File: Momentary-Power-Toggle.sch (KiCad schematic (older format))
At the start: 14 parts, among them J1 PWR_C, J2 PWR_2, J3 BT-, Q1 IRF7317PbF, SW1 ON / OFF Button

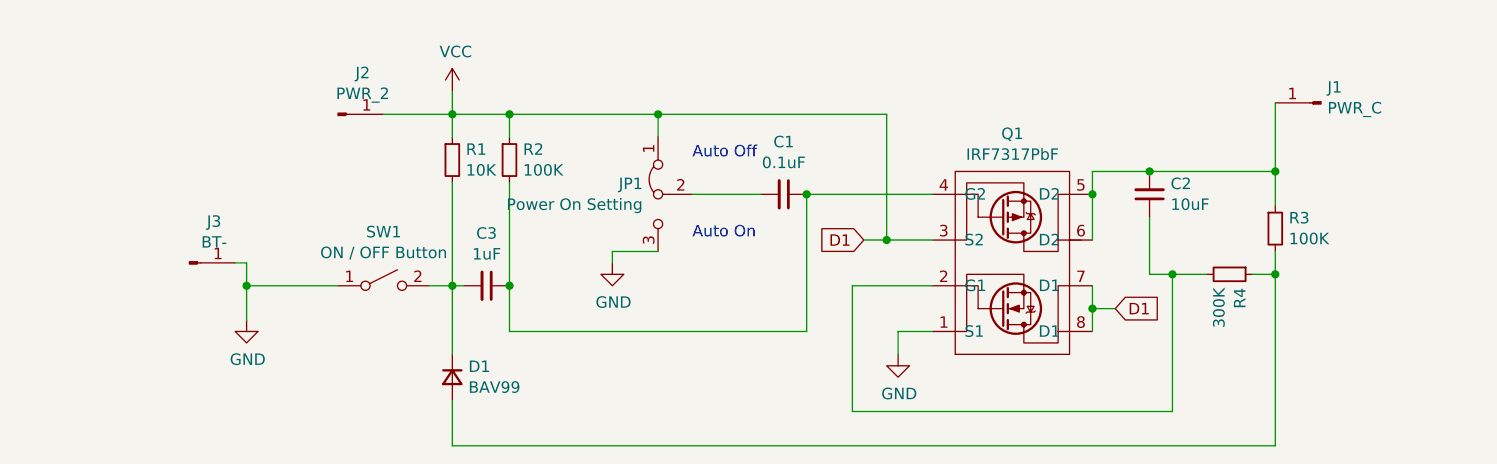
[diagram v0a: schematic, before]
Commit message: Add files via upload
fixed schematic error
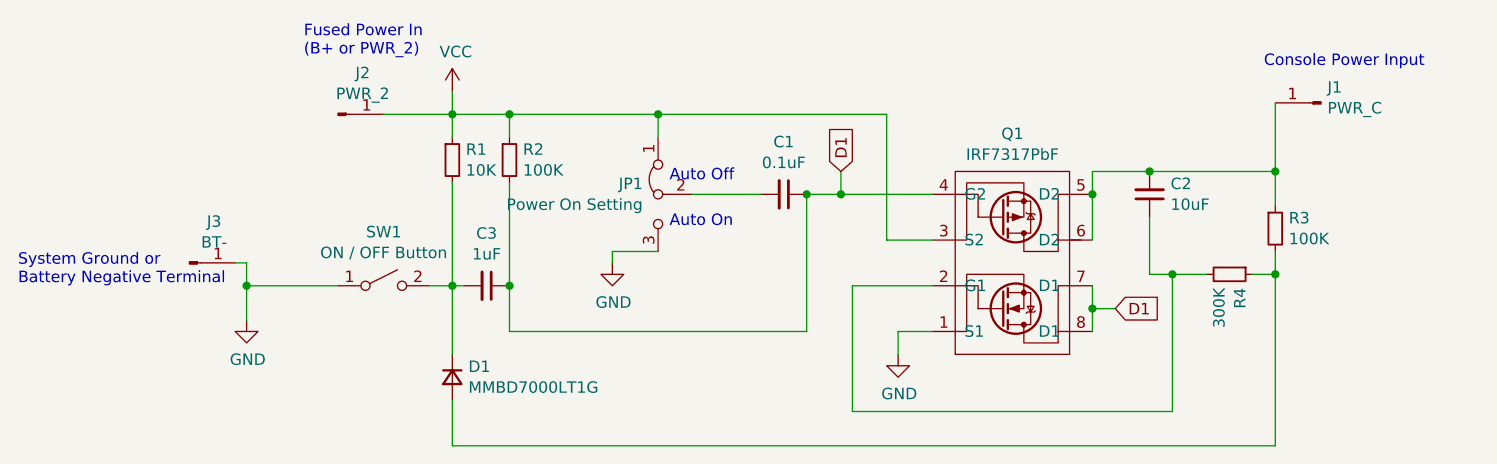
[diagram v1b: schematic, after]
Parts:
- D1: value BAV99 -> MMBD7000LT1G
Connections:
- net VCC: no longer Q1.7 (D1), Q1.8 (D1)
- net D1: now reaches C1.1, C3.1, Q1.4 (G2), R2.2
- net D1: now also Q1.7 (D1), Q1.8 (D1)
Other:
- note added: "Console Power Input"
- note added: "Fused Power In\n(B+ or PWR_2)"
- note added: "System Ground or \nBattery Negative Terminal"
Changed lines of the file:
@@
 P 3550 3850
 F 0 "D1" V 3504 3920 50  0000 L CNN
-F 1 "BAV99" V 3595 3920 50  0000 L CNN
+F 1 "MMBD7000LT1G" V 3595 3920 50  0000 L CNN
 F 2 "Diode_SMD:D_SOT-23_ANK" V 3550 3850 50  0001 C CNN
 F 3 "~" V 3550 3850 50  0001 C CNN
@@
 	1    0    0    -1
 $EndComp
-Text Notes 4600 3250 0    50   ~ 0
+Text Notes 4500 3200 0    50   ~ 0
 Auto On
-Text Notes 4600 2900 0    50   ~ 0
+Text Notes 4500 3000 0    50   ~ 0
 Auto Off
 $Comp
@@
 	5450 3250 5650 3250
 Wire Wire Line
-	5650 3050 5100 3050
+	5650 3050 5250 3050
 Wire Wire Line
 	6350 3250 6350 3050
@@
 Wire Wire Line
 	6350 3550 6350 3650
-Text GLabel 5350 3250 0    50   Input ~ 0
+Text GLabel 5250 2950 1    50   Input ~ 0
 D1
-Wire Wire Line
-	5350 3250 5450 3250
-Connection ~ 5450 3250
 Wire Wire Line
 	6600 3150 6600 3400
@@
 Wire Wire Line
 	3250 2700 3550 2700
+Text Notes 7100 2500 0    50   ~ 0
+Console Power Input
+Text Notes 1650 3450 0    50   ~ 0
+System Ground or \nBattery Negative Terminal
+Text Notes 2900 2450 0    50   ~ 0
+Fused Power In\n(B+ or PWR_2)
+Wire Wire Line
+	5250 2950 5250 3050
+Connection ~ 5250 3050
+Wire Wire Line
+	5250 3050 5100 3050
 $EndSCHEMATC

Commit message: general cleanup
defuckulated the repository by removing obsolete board configs, updating schematic image, condensing readmes, etc
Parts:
- removed JP1: Power On Setting, Jumper:SolderJumper-3_P1.3mm_Bridged2Bar12_RoundedPad1.0x1.5mm_NumberLabels, symbol Jumper:Jumper_3_Bridged12
- removed SW1: ON / OFF Button, Button_Switch_THT:SW_Tactile_SPST_Angled_PTS645Vx83-2LFS, symbol Switch:SW_SPST
- added J4: GND, TestPoint:TestPoint_Pad_1.5x1.5mm, symbol Connector:Conn_01x01_Male
- J3: value BT- -> BTN
- Q1: symbol misc:IRF7317PbF -> Momentary-Power-Toggle-rescue:IRF7317PbF-misc
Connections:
- net GND: now also J4.1 (Pin_1); no longer J3.1 (Pin_1)
- net VCC: now also C1.2
- net at C3.2, D1.1 (K), R1.2: now also J3.1 (Pin_1)
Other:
- note added: "Button to System \nGround or Battery \nNegative Terminal"
- note removed: "Auto Off"
- note removed: "Auto On"
- note removed: "System Ground or \nBattery Negative Terminal"
- moved on the sheet: J3
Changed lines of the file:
@@
-$EndComp
-$Comp
-L power:GND #PWR03
-U 1 1 5F3F1AD6
-P 2650 3600
-F 0 "#PWR03" H 2650 3350 50  0001 C CNN
-F 1 "GND" H 2655 3427 50  0000 C CNN
-F 2 "" H 2650 3600 50  0001 C CNN
-F 3 "" H 2650 3600 50  0001 C CNN
-	1    2650 3600
-	1    0    0    -1
-$EndComp
-$Comp
-L Switch:SW_SPST SW1
-U 1 1 5F3F1E0E
-P 3250 3450
-F 0 "SW1" H 3250 3685 50  0000 C CNN
-F 1 "ON / OFF Button" H 3250 3594 50  0000 C CNN
-F 2 "Button_Switch_THT:SW_Tactile_SPST_Angled_PTS645Vx83-2LFS" H 3250 3450 50  0001 C CNN
-F 3 "~" H 3250 3450 50  0001 C CNN
-	1    3250 3450
-	1    0    0    -1
 $EndComp
 $Comp
@@
 $EndComp
 $Comp
-L Jumper:Jumper_3_Bridged12 JP1
-U 1 1 5F3F302E
-P 4450 3050
-F 0 "JP1" V 4404 3117 50  0000 L CNN
-F 1 "Power On Setting" V 4495 3117 50  0000 L CNN
-F 2 "Jumper:SolderJumper-3_P1.3mm_Bridged2Bar12_RoundedPad1.0x1.5mm_NumberLabels" H 4450 3050 50  0001 C CNN
-F 3 "~" H 4450 3050 50  0001 C CNN
-	1    4450 3050
-	0    -1   1    0
-$EndComp
-$Comp
 L Device:D_Small D1
 U 1 1 5F3F351C
@@
 $EndComp
 $Comp
-L misc:IRF7317PbF Q1
+L Momentary-Power-Toggle-rescue:IRF7317PbF-misc Q1
 U 1 1 5F3FED7F
 P 6000 3300
@@
 	1    0    0    1
 $EndComp
-Wire Wire Line
-	3050 3450 2650 3450
 $Comp
 L Device:R_Small R2
@@
 	1    0    0    -1
 $EndComp
-Text Notes 4500 3200 0    50   ~ 0
-Auto On
-Text Notes 4500 3000 0    50   ~ 0
-Auto Off
 $Comp
 L Device:C_Small C1
@@
 	1    5000 3050
 	0    1    1    0
-$EndComp
-$Comp
-L power:GND #PWR02
-U 1 1 5F403AD7
-P 4250 3350
-F 0 "#PWR02" H 4250 3100 50  0001 C CNN
-F 1 "GND" H 4255 3177 50  0000 C CNN
-F 2 "" H 4250 3350 50  0001 C CNN
-F 3 "" H 4250 3350 50  0001 C CNN
-	1    4250 3350
-	1    0    0    -1
 $EndComp
 $Comp
@@
 	3550 4150 7150 4150
 Wire Wire Line
-	4250 3350 4250 3300
-Wire Wire Line
-	4250 3300 4450 3300
-Wire Wire Line
 	5450 3250 5650 3250
 Wire Wire Line
@@
 	3550 2600 3550 2700
 Wire Wire Line
-	4600 3050 4900 3050
-Wire Wire Line
 	5100 3050 5100 3650
 Wire Wire Line
@@
 Wire Wire Line
 	3800 2700 3550 2700
-Wire Wire Line
-	4450 2700 4450 2800
 Connection ~ 4450 2700
 Wire Wire Line
@@
 L Connector:Conn_01x01_Male J3
 U 1 1 5F42A93A
-P 2400 3350
-F 0 "J3" H 2508 3531 50  0000 C CNN
-F 1 "BT-" H 2508 3440 50  0000 C CNN
-F 2 "TestPoint:TestPoint_Pad_1.5x1.5mm" H 2400 3350 50  0001 C CNN
-F 3 "~" H 2400 3350 50  0001 C CNN
-	1    2400 3350
-	1    0    0    -1
-$EndComp
-Wire Wire Line
-	2600 3350 2650 3350
-Wire Wire Line
-	2650 3350 2650 3450
-Connection ~ 2650 3450
-Wire Wire Line
-	2650 3600 2650 3450
+P 3250 3450
+F 0 "J3" H 3358 3631 50  0000 C CNN
+F 1 "BTN" H 3358 3540 50  0000 C CNN
+F 2 "TestPoint:TestPoint_Pad_1.5x1.5mm" H 3250 3450 50  0001 C CNN
+F 3 "~" H 3250 3450 50  0001 C CNN
+	1    3250 3450
+	1    0    0    -1
+$EndComp
 Wire Wire Line
 	7150 2650 7150 2950
@@
 Text Notes 7100 2500 0    50   ~ 0
 Console Power Input
-Text Notes 1650 3450 0    50   ~ 0
-System Ground or \nBattery Negative Terminal
+Text Notes 2450 3550 0    50   ~ 0
+Button to System \nGround or Battery \nNegative Terminal
 Text Notes 2900 2450 0    50   ~ 0
 Fused Power In\n(B+ or PWR_2)
@@
 Wire Wire Line
 	5250 3050 5100 3050
+Wire Wire Line
+	4450 3050 4900 3050
+Wire Wire Line
+	4450 2700 4450 3050
+$Comp
+L power:GND #PWR0101
+U 1 1 5F68BE7D
+P 2250 3450
+F 0 "#PWR0101" H 2250 3200 50  0001 C CNN
+F 1 "GND" H 2255 3277 50  0000 C CNN
+F 2 "" H 2250 3450 50  0001 C CNN
+F 3 "" H 2250 3450 50  0001 C CNN
+	1    2250 3450
+	1    0    0    -1
+$EndComp
+$Comp
+L Connector:Conn_01x01_Male J4
+U 1 1 5F68C2F5
+P 1950 3350
+F 0 "J4" H 2058 3531 50  0000 C CNN
+F 1 "GND" H 2058 3440 50  0000 C CNN
+F 2 "TestPoint:TestPoint_Pad_1.5x1.5mm" H 1950 3350 50  0001 C CNN
+F 3 "~" H 1950 3350 50  0001 C CNN
+	1    1950 3350
+	1    0    0    -1
+$EndComp
+Wire Wire Line
+	2250 3450 2250 3350
+Wire Wire Line
+	2250 3350 2150 3350
 $EndSCHEMATC
